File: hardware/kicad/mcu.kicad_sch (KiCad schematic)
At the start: 12 parts, among them J1 C2_DEBUG, U5 EFM8BB21F16G-C(QSOP24)

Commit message: Filter bank F7 retuned for the pad capacitance; LCSC codes for every fitted part; C10/J1/TP1/TP6 DNP
F7 (70/23cm HPF): C701/C703 12 pF, C702 6.8 pF, L701/L702 10 nH (was 8.2p/4.7p/15n), from the
openEMS lane N-port co-simulation (simu/f7_retune.py). filters.LAYOUT_TUNED carries the values.
L403/L404: Murata LQW18ANR33G00D C162651 (ceramic core) replaces LQW18CAR33J00D.
New codes, checked on JLC/LCSC (EasyEDA API) 2026-10-28: 12pF C38523, 6.8pF C1679, 10nH C15666,
820pF C701305, 1.5uH C317997, 2.2uH C41651, 4.7uH C139136.
Schematic sheets patched in place (build.py writes random uuids; the routed board links to the
current ones); build.py carries the same changes.

Co-Authored-By: Claude Opus 5.5 <noreply@anthropic.com>
Claude-Session: https://claude.ai/code/session_01YRUiF8Vp4242sya9Xyg3TV
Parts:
- J1, TP1, TP6: now not fitted
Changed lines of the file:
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@@
     (in_bom yes)
     (on_board yes)
-    (dnp no)
+    (dnp yes)
     (property "Reference" "J1"
       (at 101.6 76.2 0)
@@
     (in_bom yes)
     (on_board yes)
-    (dnp no)
+    (dnp yes)
     (property "Reference" "TP6"
       (at 111.76 149.86 0)
@@
     (in_bom yes)
     (on_board yes)
-    (dnp no)
+    (dnp yes)
     (property "Reference" "TP1"
       (at 124.46 167.64 0)

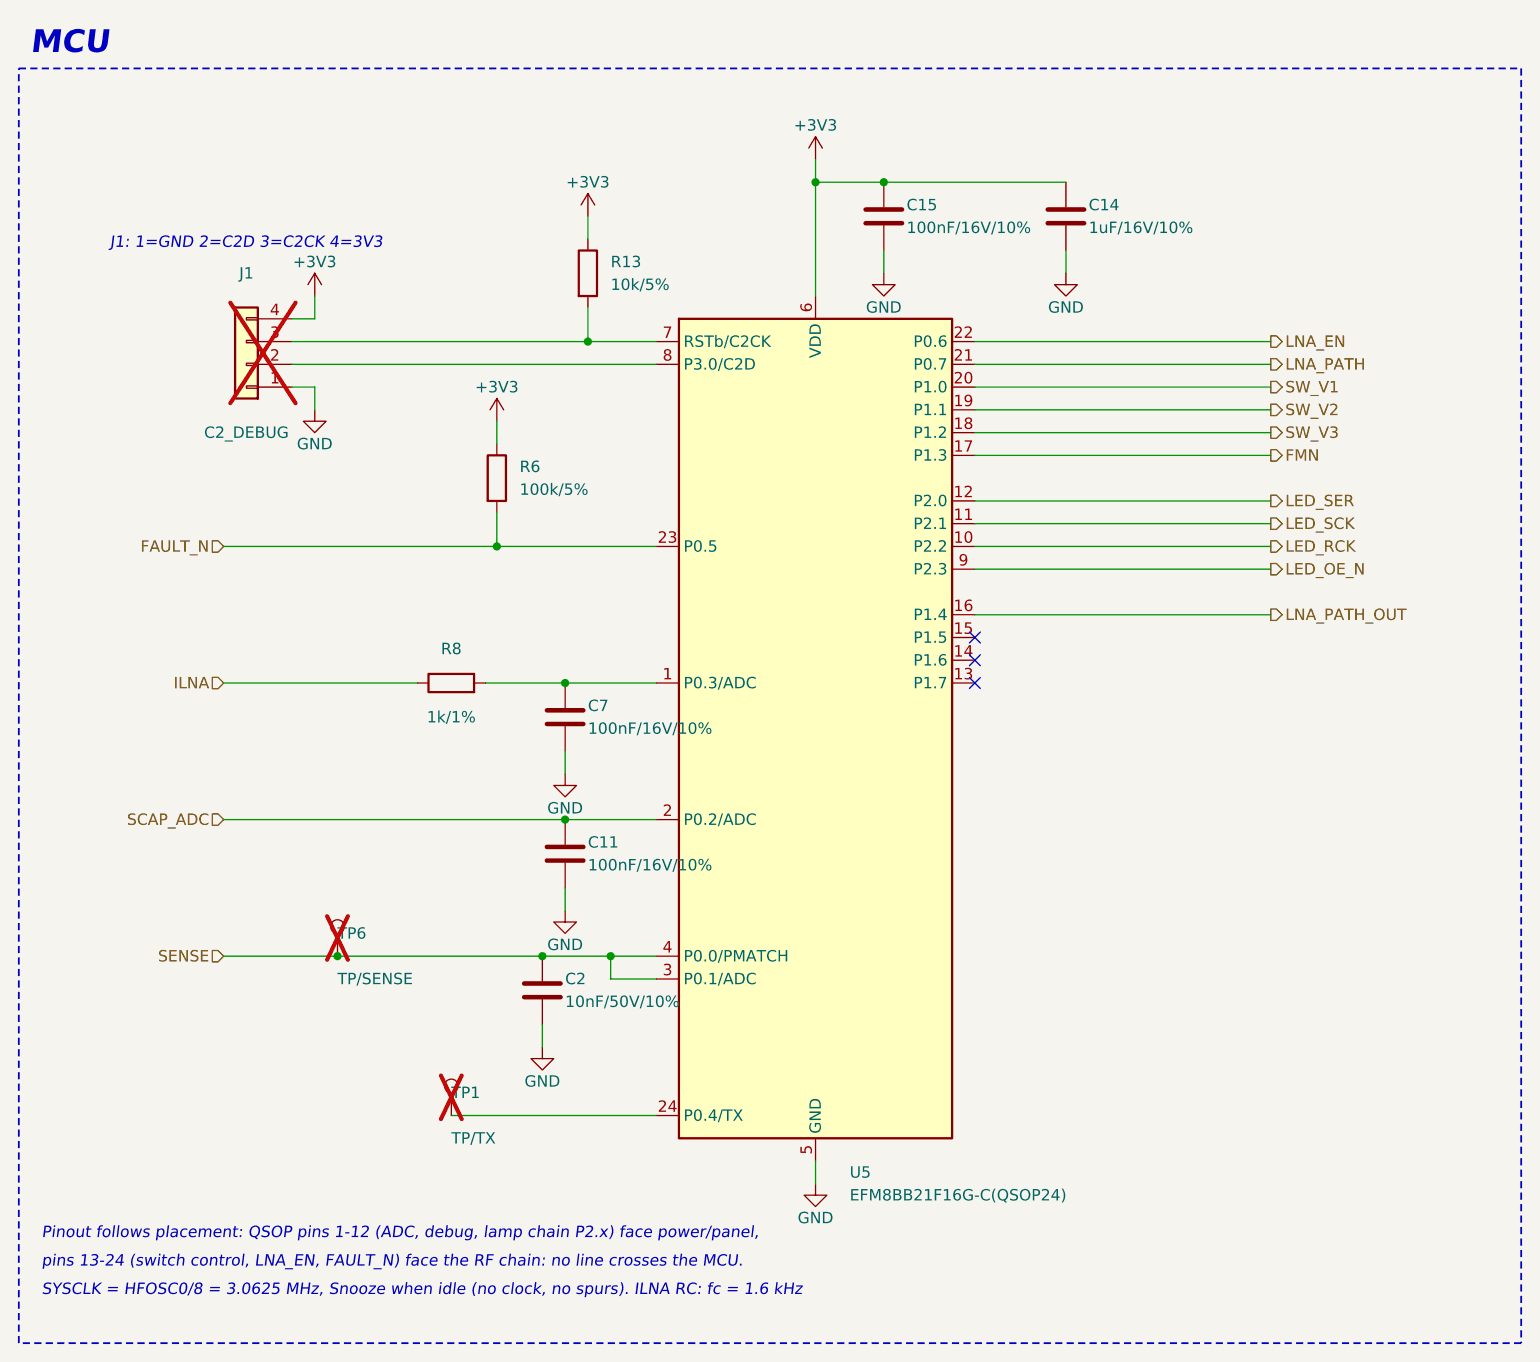
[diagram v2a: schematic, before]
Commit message: MCU to EFM8BB21F16G-C-QFN20 (QSOP24 end of life), BWSMA-KE-P001 edge SMA, Brightking GDT
U5: QFN20, all 16 port pins used. TP_TX test point dropped; LED_OE_N on P0.4, lamp chain on
P1.4-P1.6, LNA_PATH_OUT on P1.3, FMN on P2.0/C2D through R30 1k (debugger overrides it).
Footprint from the LCSC C80713 land pattern. Firmware HAL and docs/hardware.md follow;
179/179 host tests pass, SDCC build OK.
J2/J3: BAT WIRELESS BWSMA-KE-P001 (C496550) edge launch, footprint from LCSC, board edge at
local x = +2.70 mm. GDT1: Brightking 4532-091-LF (C78323), same 1812 land pattern.
check.py: netlist matches the intent.

Co-Authored-By: Claude Opus 5.5 <noreply@anthropic.com>
Claude-Session: https://claude.ai/code/session_01YRUiF8Vp4242sya9Xyg3TV
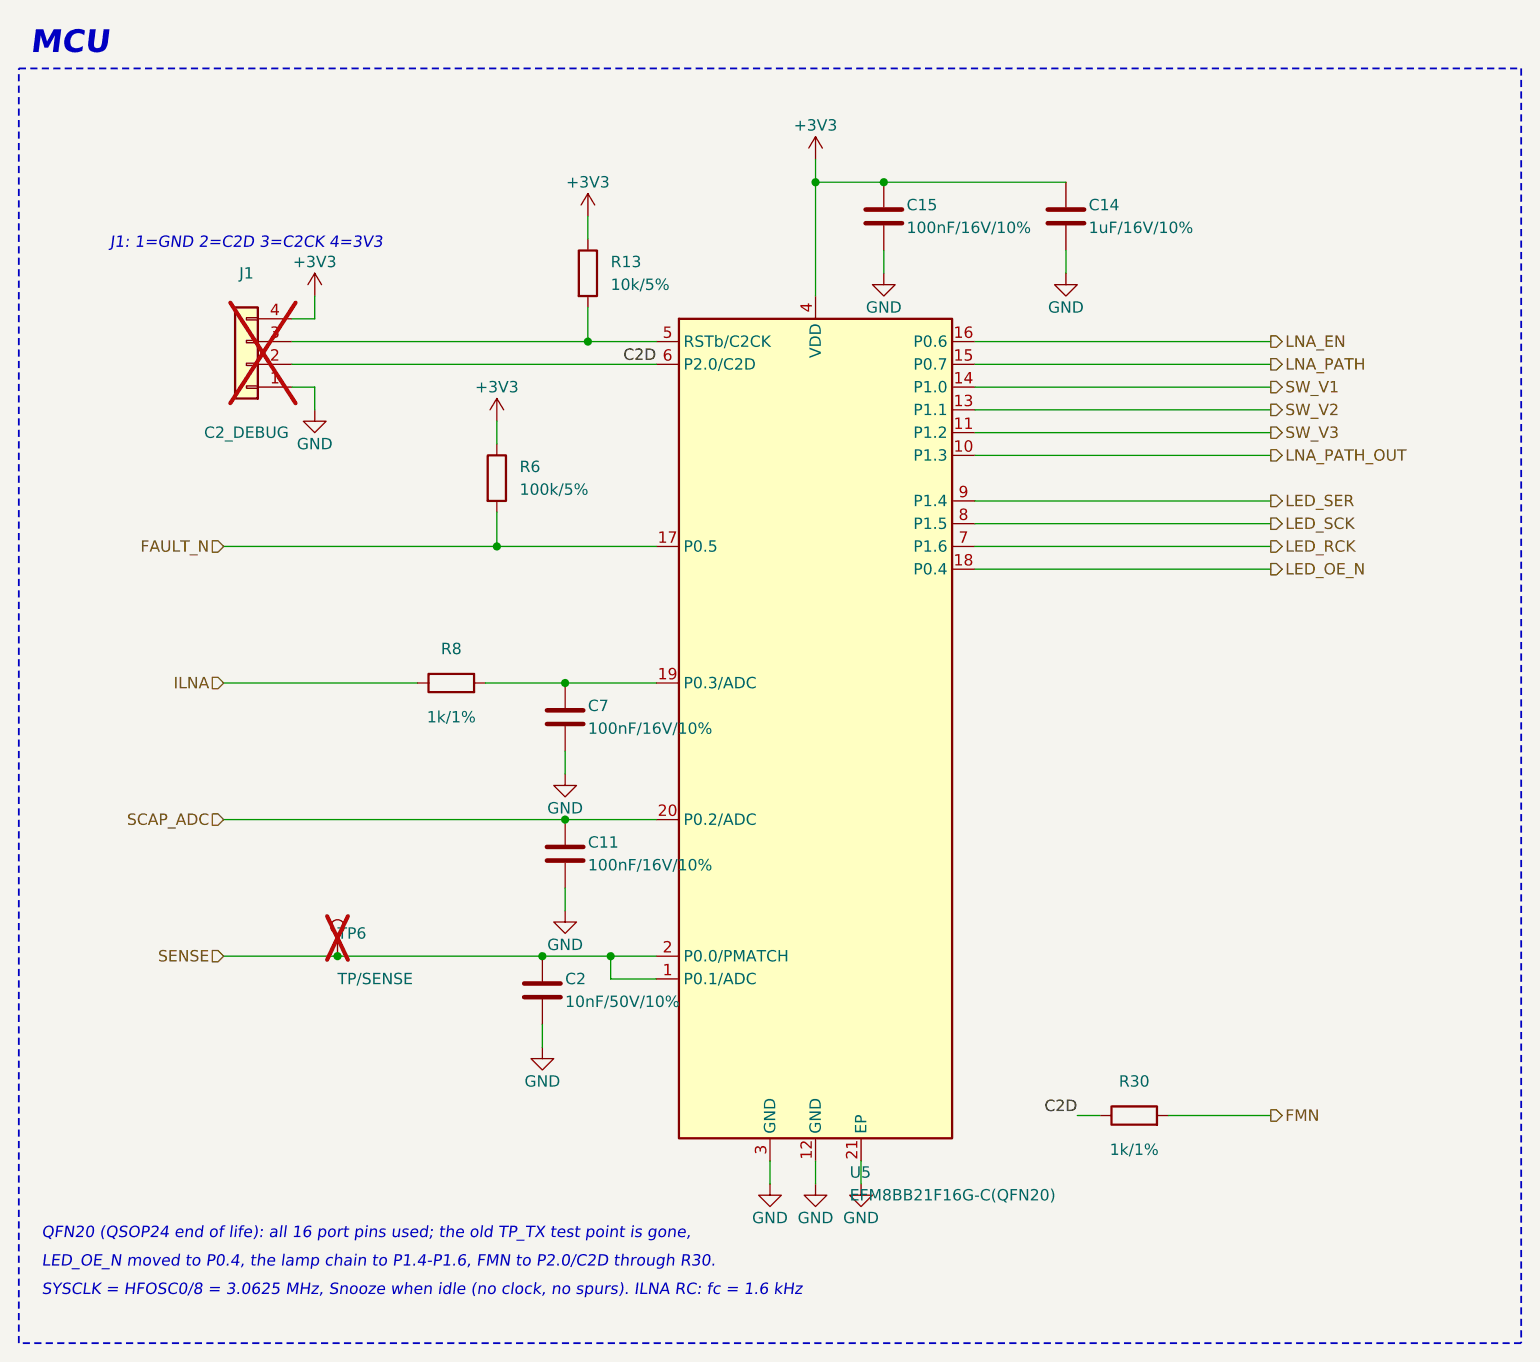
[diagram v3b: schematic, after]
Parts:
- removed TP1: TP/TX, TestPoint:TestPoint_Pad_D1.0mm, symbol Connector:TestPoint
- removed U5: EFM8BB21F16G-C(QSOP24), Package_SO:QSOP-24_3.9x8.7mm_P0.635mm, symbol coaxolotl:EFM8BB21F16G-C-QSOP24
- added R30: 1k/1%, Resistor_SMD:R_0603_1608Metric, symbol Device:R
- added U5: EFM8BB21F16G-C(QFN20), coaxolotl:EFM8_QFN-20-1EP_3x3mm_P0.5mm_EP1.7x1.7mm, symbol coaxolotl:EFM8BB21F16G-C-QFN20
- C11: Place U5.2 -> U5.20
- C14: Place U5.6 -> U5.4
- C15: Place U5.6 (closest) -> U5.4 (closest)
- C2: Place U5.4 -> U5.2
- C7, R8: Place U5.1 -> U5.19
- R13: Place U5.7 -> U5.5
- R6: Place U5.23 -> U5.17
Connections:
- net +3V3: now also U5.4 (VDD)
- net FAULT_N: now also U5.17 (P0.5)
- net FMN: now also R30.2
- net GND: now also U5.12 (GND), U5.21 (EP), U5.3 (GND)
- net LED_OE_N: now also U5.18 (P0.4)
- net LED_RCK: now also U5.7 (P1.6)
- net LED_SCK: now also U5.8 (P1.5)
- net LED_SER: now also U5.9 (P1.4)
- net LNA_EN: now also U5.16 (P0.6)
- net LNA_PATH: now also U5.15 (P0.7)
- net LNA_PATH_OUT: now also U5.10 (P1.3)
- net SCAP_ADC: now also U5.20 (P0.2/ADC)
- net SENSE: now also U5.1 (P0.1/ADC), U5.2 (P0.0/PMATCH)
- net SW_V1: now also U5.14 (P1.0)
- net SW_V2: now also U5.13 (P1.1)
- net SW_V3: now also U5.11 (P1.2)
- net at C7.1, R8.2: now also U5.19 (P0.3/ADC)
- net at J1.3 (Pin_3), R13.2: now also U5.5 (RSTb/C2CK)
- net C2D: now reaches J1.2 (Pin_2)
- net C2D: now also R30.1, U5.6 (P2.0/C2D)
- no-connect marks 3 -> 0
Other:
- note added: "LED_OE_N moved to P0.4, the lamp chain to P1.4-P1.6, FMN to P2.0/C2D through R30."
- note added: "QFN20 (QSOP24 end of life): all 16 port pins used; the old TP_TX test point is gone,"
- note removed: "Pinout follows placement: QSOP pins 1-12 (ADC, debug, lamp chain P2.x) face power/panel,"
- note removed: "pins 13-24 (switch control, LNA_EN, FAULT_N) face the RF chain: no line crosses the MCU."
